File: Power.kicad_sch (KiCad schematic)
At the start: 87 parts, among them U1 TPS546D24ARVFR, U3 TPSM861253RDXR, U4 TPS546D24ARVFR, U5 L78L05_SOT89

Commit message: lots of routing
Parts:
- removed C25, C4: 1uF, Capacitor_SMD:C_0402_1005Metric, symbol Device:C_Small
- removed C26, C5: 4.7nF, Capacitor_SMD:C_0402_1005Metric, symbol Device:C_Small
- removed C27, C6: 2.2nF, Capacitor_SMD:C_0402_1005Metric, symbol Device:C_Small
- removed R10, R12, R9: R, Resistor_SMD:R_0402_1005Metric, symbol Device:R_Small_US
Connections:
- no-connect marks 6 -> 7
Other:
- title: bitaxeGamma Turbo -> bitaxeNaja
- moved on the sheet: C1, C2, C22, C23, C24, C3

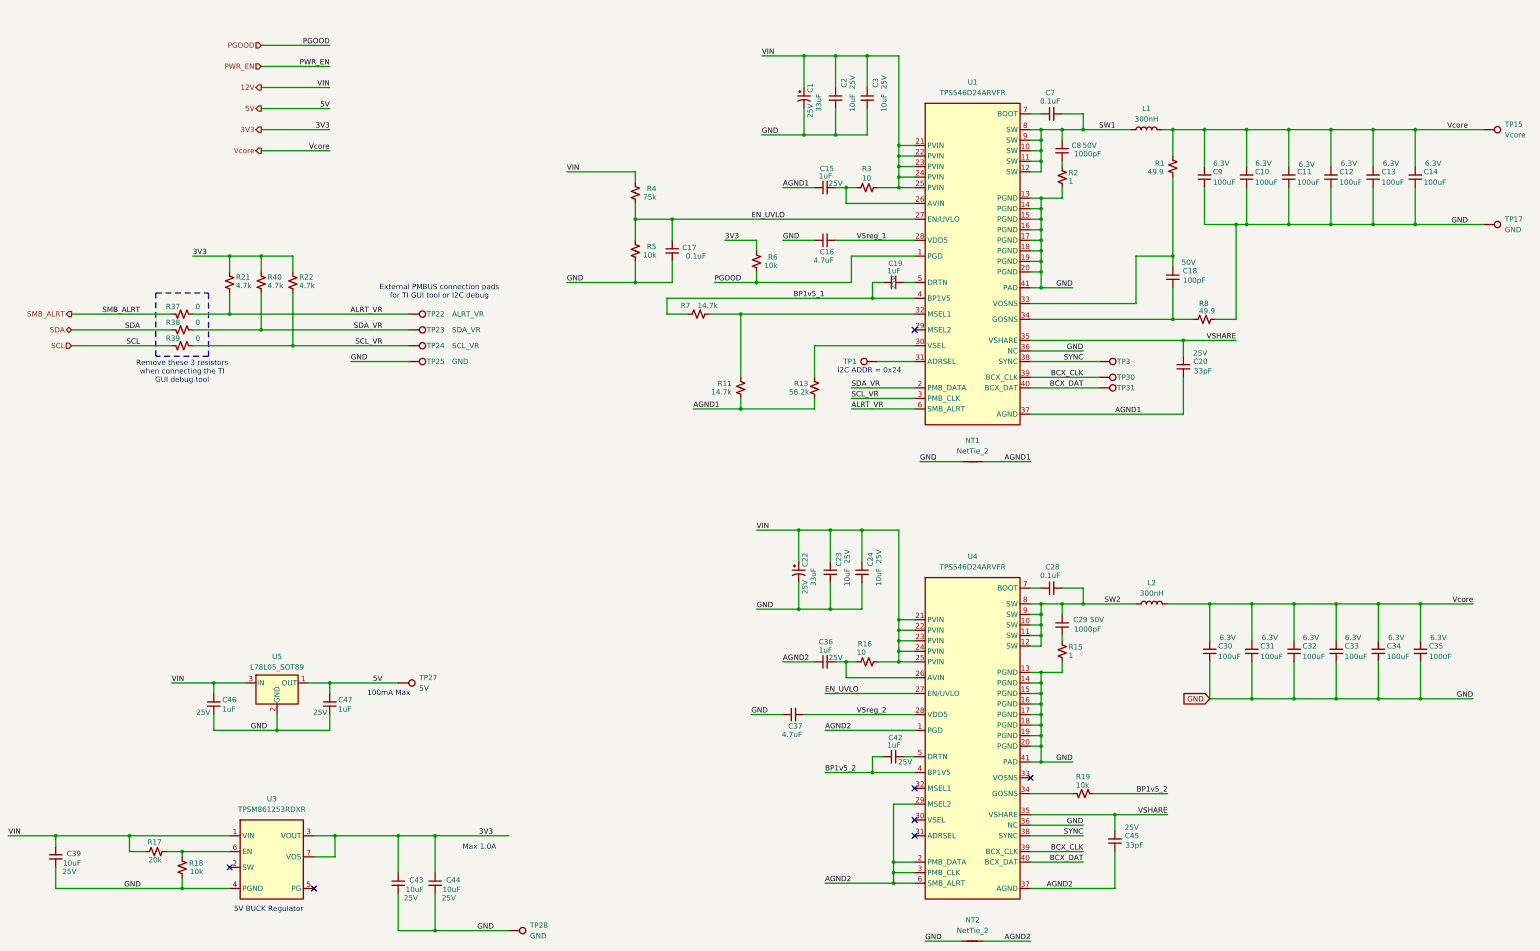
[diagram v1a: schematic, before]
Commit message: placed and routed and DRC'd. updated TPS546 for 1.0V output.
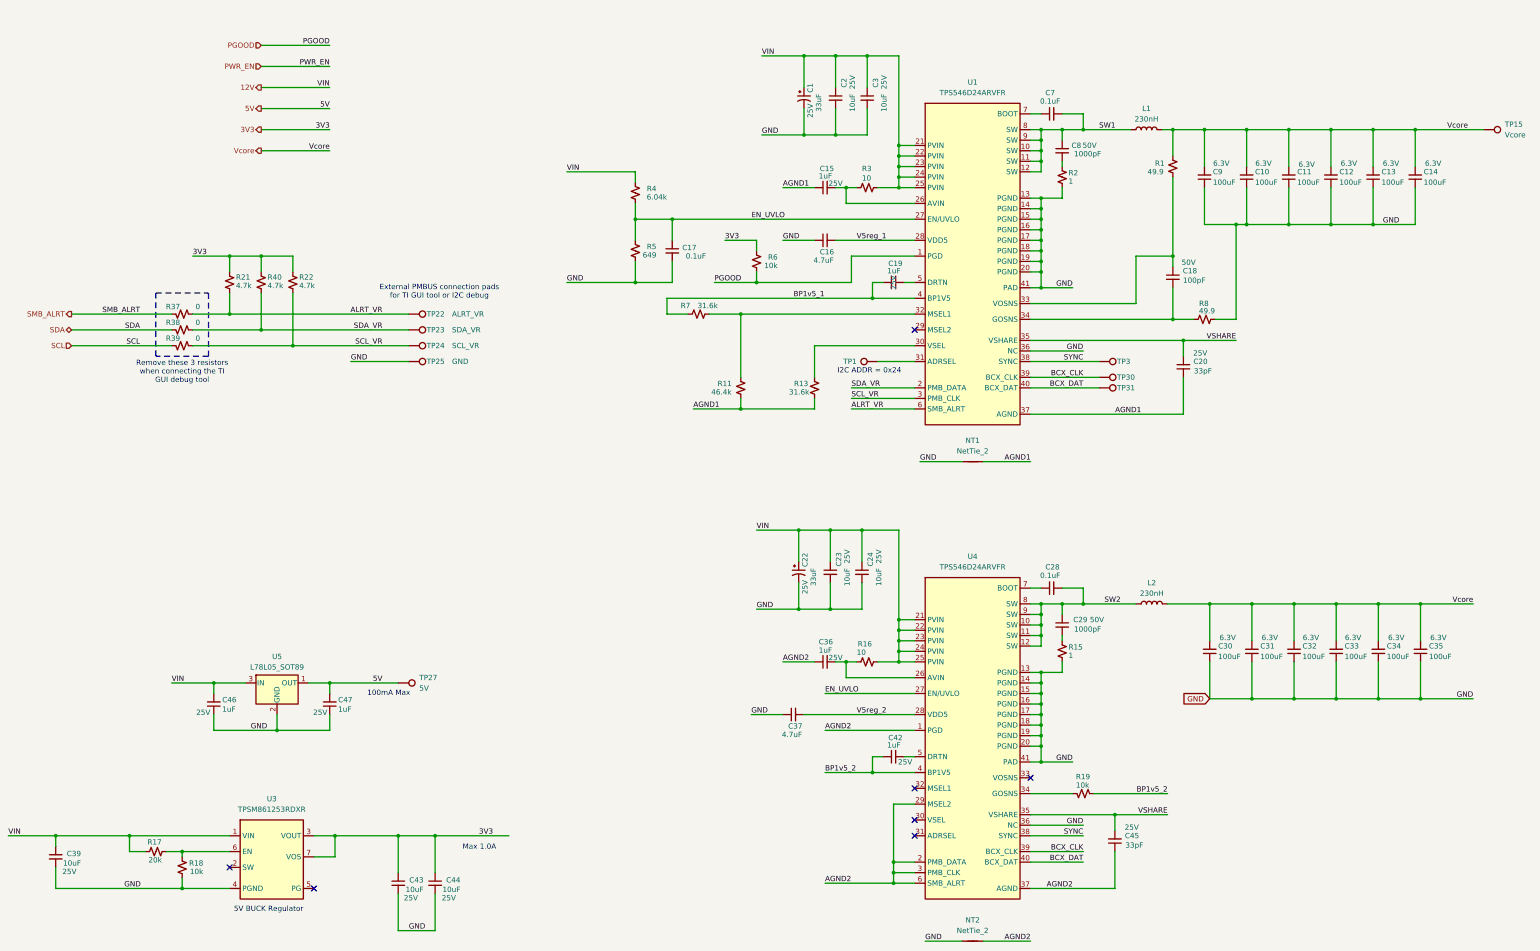
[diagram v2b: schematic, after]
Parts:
- removed TP17, TP28: GND, TestPoint:TestPoint_Pad_D1.5mm, symbol Connector:TestPoint
- L1, L2: value 300nH -> 230nH; footprint bitaxe:SLC1175-271MEC_COC -> bitaxe:FP1107R1; DK (none) -> 283-FP1107R1-R23-RCT-ND; PARTNO SLC1175-271MEC -> FP1107R1-R23-R
- R11: value 14.7k -> 46.4k; DK YAG5262CT-ND -> (none); PARTNO AC0402FR-0714K7L -> (none)
- R13: value 56.2k -> 31.6k; DK YAG3187CT-ND -> (none); PARTNO RC0402FR-0756K2L -> (none)
- R4: value 75k -> 6.04k; DK 311-75KLRCT-ND -> (none); PARTNO RC0402FR-0775KL -> (none)
- R5: value 10k -> 649; DK 311-10KJRCT-ND -> (none); PARTNO RC0402JR-0710KL -> (none)
- R7: value 14.7k -> 31.6k; DK YAG5262CT-ND -> (none); PARTNO AC0402FR-0714K7L -> (none)
- TP22, TP23, TP24, TP25: footprint TestPoint:TestPoint_Pad_D1.5mm -> TestPoint:TestPoint_Pad_D1.0mm
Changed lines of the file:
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@@
 	)
 	(junction
-		(at 361.95 77.47)
-		(diameter 0)
-		(color 0 0 0 0)
-	)
-	(junction
 		(at 271.78 198.12)
 		(diameter 0)
@@
 	)
 	(junction
-		(at 125.73 247.65)
-		(diameter 0)
-		(color 0 0 0 0)
-	)
-	(junction
 		(at 351.79 77.47)
 		(diameter 0)
@@
 	(wire
 		(pts
-			(xy 361.95 77.47) (xy 378.46 77.47)
-		)
-		(stroke
-			(width 0)
-			(type default)
-		)
-	)
-	(wire
-		(pts
 			(xy 241.3 217.17) (xy 236.22 217.17)
 		)
@@
 	(wire
 		(pts
-			(xy 125.73 247.65) (xy 143.51 247.65)
-		)
-		(stroke
-			(width 0)
-			(type default)
-		)
-	)
-	(wire
-		(pts
 			(xy 219.71 190.5) (xy 241.3 190.5)
 		)
@@
 	)
 	(label "GND"
-		(at 135.89 247.65 0)
+		(at 119.38 247.65 0)
 		(effects
 			(font
@@
 	)
 	(label "GND"
-		(at 374.65 77.47 180)
+		(at 358.14 77.47 180)
 		(effects
 			(font
@@
 			)
 		)
-		(property "Value" "75k"
-			(at 179.07 70.866 0)
+		(property "Value" "6.04k"
+			(at 181.61 70.866 0)
 			(effects
 				(font
@@
 			)
 		)
-		(property "Datasheet" "https://www.yageo.com/upload/media/product/products/datasheet/rchip/PYu-RC_Group_51_RoHS_L_12.pdf"
+		(property "Datasheet" ""
 			(at 173.99 69.85 0)
 			(effects
@@
 			)
 		)
-		(property "PARTNO" "RC0402FR-0775KL"
+		(property "PARTNO" ""
 			(at 173.99 69.85 0)
 			(effects
@@
 			)
 		)
-		(property "DK" "311-75KLRCT-ND"
+		(property "DK" ""
 			(at 173.99 69.85 0)
 			(effects
@@
 			)
 		)
-		(property "Value" "14.7k"
+		(property "Value" "31.6k"
 			(at 188.976 97.028 90)
 			(effects
@@
 			)
 		)
-		(property "Datasheet" "https://www.yageo.com/upload/media/product/products/datasheet/rchip/PYu-RC_Group_51_RoHS_L_12.pdf"
+		(property "Datasheet" ""
 			(at 189.23 99.06 0)
 			(effects
@@
 			)
 		)
-		(property "PARTNO" "AC0402FR-0714K7L"
+		(property "PARTNO" ""
 			(at 189.23 99.06 90)
 			(effects
@@
 			)
 		)
-		(property "DK" "YAG5262CT-ND"
+		(property "DK" ""
 			(at 189.23 99.06 90)
 			(effects
@@
 			)
 		)
-		(property "Value" "14.7k"
+		(property "Value" "46.4k"
 			(at 192.278 117.856 0)
 			(effects
@@
 			)
 		)
-		(property "Datasheet" "https://www.yageo.com/upload/media/product/products/datasheet/rchip/PYu-RC_Group_51_RoHS_L_12.pdf"
+		(property "Datasheet" ""
 			(at 199.39 116.84 0)
 			(effects
@@
 			)
 		)
-		(property "PARTNO" "AC0402FR-0714K7L"
+		(property "PARTNO" ""
 			(at 199.39 116.84 90)
 			(effects
@@
 			)
 		)
-		(property "DK" "YAG5262CT-ND"
+		(property "DK" ""
 			(at 199.39 116.84 90)
 			(effects
@@
 			)
 		)
-		(property "Footprint" "TestPoint:TestPoint_Pad_D1.5mm"
+		(property "Footprint" "TestPoint:TestPoint_Pad_D1.0mm"
 			(at 119.38 111.76 0)
 			(effects
@@
 			)
 		)
-		(property "Footprint" "TestPoint:TestPoint_Pad_D1.5mm"
+		(property "Footprint" "TestPoint:TestPoint_Pad_D1.0mm"
 			(at 119.38 115.57 0)
 			(effects
@@
 	)
 	(symbol
-		(lib_id "Connector:TestPoint")
-		(at 143.51 247.65 270)
-		(unit 1)
-		(exclude_from_sim no)
-		(in_bom no)
-		(on_board yes)
-		(dnp no)
-		(fields_autoplaced yes)
-		(property "Reference" "TP28"
-			(at 148.59 246.3799 90)
-			(effects
-				(font
-					(size 1.27 1.27)
-				)
-				(justify left)
-			)
-		)
-		(property "Value" "GND"
-			(at 148.59 248.9199 90)
-			(effects
-				(font
-					(size 1.27 1.27)
-				)
-				(justify left)
-			)
-		)
-		(property "Footprint" "TestPoint:TestPoint_Pad_D1.5mm"
-			(at 143.51 252.73 0)
-			(effects
-				(font
-					(size 1.27 1.27)
-				)
-				(hide yes)
-			)
-		)
-		(property "Datasheet" "~"
-			(at 143.51 252.73 0)
-			(effects
-				(font
-					(size 1.27 1.27)
-				)
-				(hide yes)
-			)
-		)
-		(property "Description" "test point"
-			(at 143.51 247.65 0)
-			(effects
-				(font
-					(size 1.27 1.27)
-				)
-				(hide yes)
-			)
-		)
-		(pin "1"
-		)
-		(instances
-			(project "BitaxeGT"
-				(path "/61fe8d2c-9301-4ad9-8caf-c47acfa835b0/24036843-8461-4d4b-b738-f953c909ed6c"
-					(reference "TP28")
-					(unit 1)
-				)
-			)
-		)
-	)
-	(symbol
 		(lib_id "Device:C_Small")
 		(at 332.74 180.34 180)
@@
 			)
 		)
-		(property "Value" "10k"
+		(property "Value" "649"
 			(at 179.07 84.836 0)
 			(effects
@@
 			)
 		)
-		(property "Datasheet" "https://www.yageo.com/upload/media/product/products/datasheet/rchip/PYu-RC_Group_51_RoHS_L_12.pdf"
+		(property "Datasheet" ""
 			(at 173.99 83.82 0)
 			(effects
@@
 			)
 		)
-		(property "PARTNO" "RC0402JR-0710KL"
+		(property "PARTNO" ""
 			(at 173.99 83.82 0)
 			(effects
@@
 			)
 		)
-		(property "DK" "311-10KJRCT-ND"
+		(property "DK" ""
 			(at 173.99 83.82 0)
 			(effects
@@
 			)
 		)
-		(property "Value" "56.2k"
+		(property "Value" "31.6k"
 			(at 215.9 117.856 0)
 			(effects
@@
 			)
 		)
-		(property "Datasheet" "https://www.yageo.com/upload/media/product/products/datasheet/rchip/PYu-RC_Group_51_RoHS_L_12.pdf"
+		(property "Datasheet" ""
 			(at 217.17 116.84 0)
 			(effects
@@
 			)
 		)
-		(property "PARTNO" "RC0402FR-0756K2L"
+		(property "PARTNO" ""
 			(at 217.17 116.84 0)
 			(effects
@@
 			)
 		)
-		(property "DK" "YAG3187CT-ND"
+		(property "DK" ""
 			(at 217.17 116.84 0)
 			(effects
@@
 			)
 		)
-		(property "Value" "300nH"
+		(property "Value" "230nH"
 			(at 297.18 52.07 90)
 			(effects
@@
 			)
 		)
-		(property "Footprint" "bitaxe:SLC1175-271MEC_COC"
+		(property "Footprint" "bitaxe:FP1107R1"
 			(at 297.18 54.61 0)
 			(effects
@@
 			)
 		)
-		(property "Datasheet" "https://products.sumida.com/products/pdf/104CDMCCDS.pdf"
+		(property "Datasheet" ""
 			(at 297.18 54.61 0)
 			(effects
@@
 			)
 		)
-		(property "PARTNO" "SLC1175-271MEC"
+		(property "PARTNO" "FP1107R1-R23-R"
 			(at 297.18 54.61 90)
 			(effects
@@
 			)
 		)
-		(property "DK" ""
+		(property "DK" "283-FP1107R1-R23-RCT-ND"
 			(at 297.18 54.61 0)
 			(effects
@@
 	(symbol
 		(lib_id "Connector:TestPoint")
-		(at 378.46 77.47 270)
-		(unit 1)
-		(exclude_from_sim no)
-		(in_bom no)
-		(on_board yes)
-		(dnp no)
-		(fields_autoplaced yes)
-		(property "Reference" "TP17"
-			(at 383.54 76.1999 90)
-			(effects
-				(font
-					(size 1.27 1.27)
-				)
-				(justify left)
-			)
-		)
-		(property "Value" "GND"
-			(at 383.54 78.7399 90)
-			(effects
-				(font
-					(size 1.27 1.27)
-				)
-				(justify left)
-			)
-		)
-		(property "Footprint" "TestPoint:TestPoint_Pad_D1.5mm"
-			(at 378.46 82.55 0)
-			(effects
-				(font
-					(size 1.27 1.27)
-				)
-				(hide yes)
-			)
-		)
-		(property "Datasheet" "~"
-			(at 378.46 82.55 0)
-			(effects
-				(font
-					(size 1.27 1.27)
-				)
-				(hide yes)
-			)
-		)
-		(property "Description" "test point"
-			(at 378.46 77.47 0)
-			(effects
-				(font
-					(size 1.27 1.27)
-				)
-				(hide yes)
-			)
-		)
-		(pin "1"
-		)
-		(instances
-			(project "BitaxeGT"
-				(path "/61fe8d2c-9301-4ad9-8caf-c47acfa835b0/24036843-8461-4d4b-b738-f953c909ed6c"
-					(reference "TP17")
-					(unit 1)
-				)
-			)
-		)
-	)
-	(symbol
-		(lib_id "Connector:TestPoint")
 		(at 119.38 102.87 270)
 		(unit 1)
@@
 			)
 		)
-		(property "Footprint" "TestPoint:TestPoint_Pad_D1.5mm"
+		(property "Footprint" "TestPoint:TestPoint_Pad_D1.0mm"
 			(at 119.38 107.95 0)
 			(effects
@@
 			)
 		)
-		(property "Footprint" "TestPoint:TestPoint_Pad_D1.5mm"
+		(property "Footprint" "TestPoint:TestPoint_Pad_D1.0mm"
 			(at 119.38 104.14 0)
 			(effects
@@
 			)
 		)
-		(property "Value" "300nH"
+		(property "Value" "230nH"
 			(at 298.45 166.37 90)
 			(effects
@@
 			)
 		)
-		(property "Footprint" "bitaxe:SLC1175-271MEC_COC"
+		(property "Footprint" "bitaxe:FP1107R1"
 			(at 298.45 168.91 0)
 			(effects
@@
 			)
 		)
-		(property "PARTNO" "SLC1175-271MEC"
+		(property "PARTNO" "FP1107R1-R23-R"
 			(at 298.45 168.91 90)
 			(effects
@@
 			)
 		)
-		(property "DK" ""
+		(property "DK" "283-FP1107R1-R23-RCT-ND"
 			(at 298.45 168.91 0)
 			(effects
@@
 					(size 1.27 1.27)
 				)
+				(hide yes)
 			)
 		)

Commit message: added checked gerbers and BOM
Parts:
- R11: DK (none) -> 311-46.4KLRCT-ND; PARTNO (none) -> RC0402FR-0746K4L
- R13, R7: DK (none) -> YAG3115CT-ND; PARTNO (none) -> RC0402FR-0731K6L
- R4: DK (none) -> RC0402FR-076K04L; PARTNO (none) -> YAG2293CT-ND
- R5: DK (none) -> YAG3206CT-ND; PARTNO (none) -> RC0402FR-07649RL
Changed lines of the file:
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@@
 			)
 		)
-		(property "PARTNO" ""
+		(property "PARTNO" "YAG2293CT-ND"
 			(at 173.99 69.85 0)
 			(effects
@@
 			)
 		)
-		(property "DK" ""
+		(property "DK" "RC0402FR-076K04L"
 			(at 173.99 69.85 0)
 			(effects
@@
 			)
 		)
-		(property "PARTNO" ""
+		(property "PARTNO" "RC0402FR-0731K6L"
 			(at 189.23 99.06 90)
 			(effects
@@
 			)
 		)
-		(property "DK" ""
+		(property "DK" "YAG3115CT-ND"
 			(at 189.23 99.06 90)
 			(effects
@@
 			)
 		)
-		(property "PARTNO" ""
+		(property "PARTNO" "RC0402FR-0746K4L"
 			(at 199.39 116.84 90)
 			(effects
@@
 			)
 		)
-		(property "DK" ""
+		(property "DK" "311-46.4KLRCT-ND"
 			(at 199.39 116.84 90)
 			(effects
@@
 			)
 		)
-		(property "PARTNO" ""
+		(property "PARTNO" "RC0402FR-07649RL"
 			(at 173.99 83.82 0)
 			(effects
@@
 			)
 		)
-		(property "DK" ""
+		(property "DK" "YAG3206CT-ND"
 			(at 173.99 83.82 0)
 			(effects
@@
 			)
 		)
-		(property "PARTNO" ""
+		(property "PARTNO" "RC0402FR-0731K6L"
 			(at 217.17 116.84 0)
 			(effects
@@
 			)
 		)
-		(property "DK" ""
+		(property "DK" "YAG3115CT-ND"
 			(at 217.17 116.84 0)
 			(effects

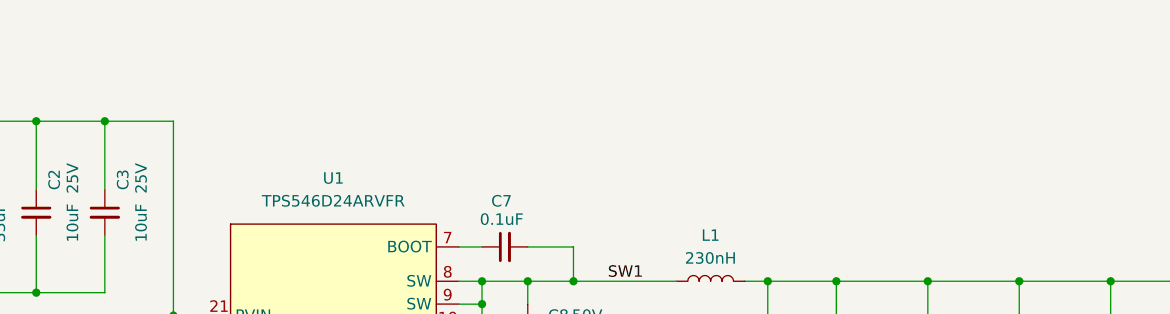
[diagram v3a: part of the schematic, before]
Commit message: added webench design
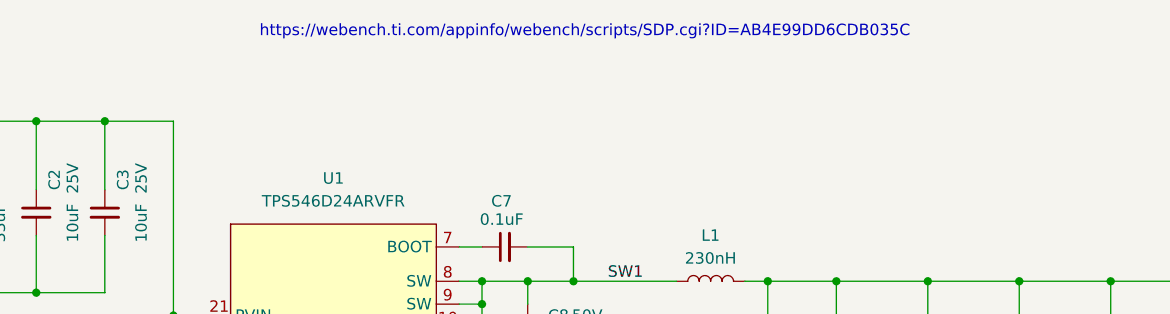
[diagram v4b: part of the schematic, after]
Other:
- note added: "https://webench.ti.com/appinfo/webench/scripts/SDP.cgi?ID=AB4E99DD6CDB035C"
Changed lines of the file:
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@@
+		)
+	)
+	(text "https://webench.ti.com/appinfo/webench/scripts/SDP.cgi?ID=AB4E99DD6CDB035C"
+		(exclude_from_sim no)
+		(at 283.21 26.924 0)
+		(effects
+			(font
+				(size 1.27 1.27)
+			)
 		)
 	)

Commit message: update to KiCad 10
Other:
- company: (none) -> bitaxeorg
